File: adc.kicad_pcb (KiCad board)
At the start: 2 copper layers, 17 parts, among them U201 ADS8665IPWR

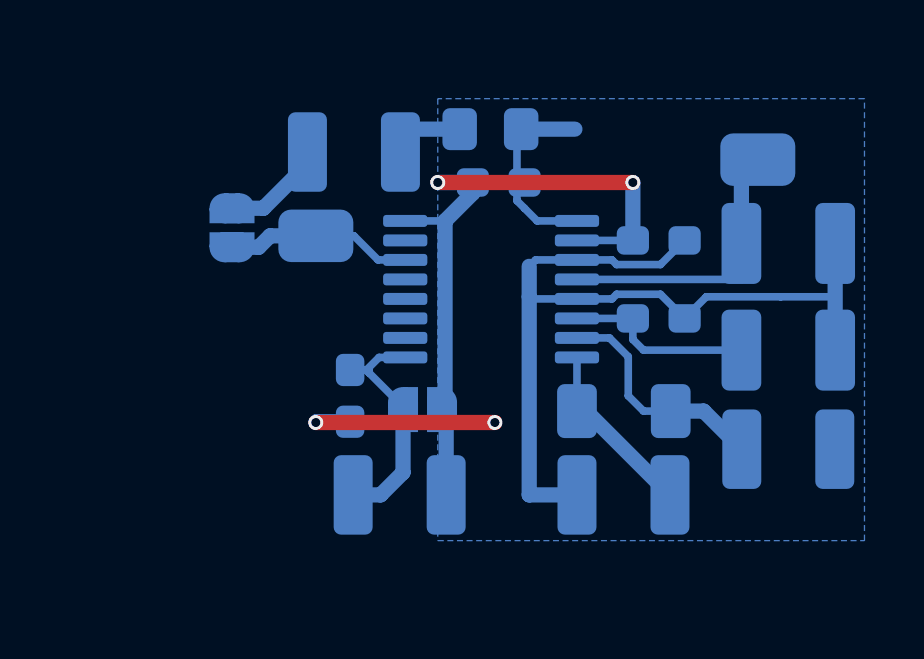
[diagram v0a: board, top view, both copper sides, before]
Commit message: add adc sub-layout
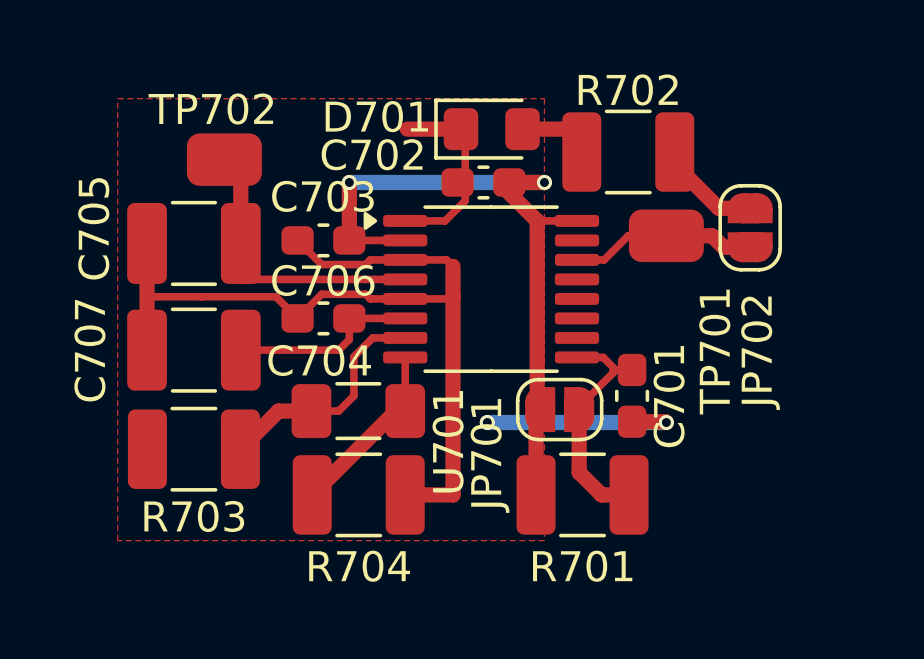
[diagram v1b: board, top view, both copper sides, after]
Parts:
- C701: renamed from C201; footprint pss:C_0603_1608Metric_Pad1.08x0.95mm_HandSolder -> meas:C_0603_1608Metric_Pad1.08x0.95mm_HandSolder; moved to F.Cu
- C702: renamed from C202; footprint pss:C_0603_1608Metric_Pad1.08x0.95mm_HandSolder -> meas:C_0603_1608Metric_Pad1.08x0.95mm_HandSolder; moved to F.Cu
- C703: renamed from C203; footprint pss:C_0603_1608Metric_Pad1.08x0.95mm_HandSolder -> meas:C_0603_1608Metric_Pad1.08x0.95mm_HandSolder; moved to F.Cu
- C704: renamed from C204; footprint pss:C_1206_3216Metric_Pad1.33x1.80mm_HandSolder -> meas:C_1206_3216Metric_Pad1.33x1.80mm_HandSolder; moved to F.Cu
- C705: renamed from C205; footprint pss:C_1210_3225Metric_Pad1.33x2.70mm_HandSolder -> meas:C_1210_3225Metric_Pad1.33x2.70mm_HandSolder; moved to F.Cu
- C706: renamed from C206; footprint pss:C_0603_1608Metric_Pad1.08x0.95mm_HandSolder -> meas:C_0603_1608Metric_Pad1.08x0.95mm_HandSolder; moved to F.Cu
- C707: renamed from C207; footprint pss:C_1210_3225Metric_Pad1.33x2.70mm_HandSolder -> meas:C_1210_3225Metric_Pad1.33x2.70mm_HandSolder; moved to F.Cu
- D701: renamed from D201; footprint pss:LED_0805_2012Metric_Pad1.15x1.40mm_HandSolder -> meas:LED_0805_2012Metric_Pad1.15x1.40mm_HandSolder; moved to F.Cu
- JP701: renamed from JP201; footprint pss:SolderJumper-2_P1.3mm_Open_RoundedPad1.0x1.5mm -> meas:SolderJumper-2_P1.3mm_Open_RoundedPad1.0x1.5mm; moved to F.Cu
- JP702: renamed from JP202; footprint pss:SolderJumper-2_P1.3mm_Bridged-Soldermask-Paste_RoundedPad1.0x1.5mm -> meas:SolderJumper-2_P1.3mm_Bridged-Soldermask-Paste_RoundedPad1.0x1.5mm; moved to F.Cu
- R701: renamed from R201; footprint pss:R_1210_3225Metric_Pad1.30x2.65mm_HandSolder -> meas:R_1210_3225Metric_Pad1.30x2.65mm_HandSolder; moved to F.Cu
- R702: renamed from R202; footprint pss:R_1210_3225Metric_Pad1.30x2.65mm_HandSolder -> meas:R_1210_3225Metric_Pad1.30x2.65mm_HandSolder; moved to F.Cu
- R703: renamed from R203; footprint pss:R_1210_3225Metric_Pad1.30x2.65mm_HandSolder -> meas:R_1210_3225Metric_Pad1.30x2.65mm_HandSolder; moved to F.Cu
- R704: renamed from R204; footprint pss:R_1210_3225Metric_Pad1.30x2.65mm_HandSolder -> meas:R_1210_3225Metric_Pad1.30x2.65mm_HandSolder; moved to F.Cu
- TP701: renamed from TP201; footprint pss:TP_0805_2012Metric -> meas:TP_0805_2012Metric; moved to F.Cu
- TP702: renamed from TP202; footprint pss:TP_0805_2012Metric -> meas:TP_0805_2012Metric; moved to F.Cu
- U701: renamed from U201; footprint pss:TSSOP-16_4.4x5mm_P0.65mm -> meas:TSSOP-16_4.4x5mm_P0.65mm; moved to F.Cu
- moved C705 19.8 mm to (65.3, 55.9), turned to 0 degrees
- moved C707 19.8 mm to (65.3, 59.4), turned to 0 degrees
- moved R703 19.8 mm to (65.3, 62.7), turned to 180 degrees
- moved TP702 17.8 mm to (66.3, 53.1), turned to 0 degrees
- moved JP702 17.3 mm to (83.8, 55.4)
- moved TP701 11.7 mm to (81.0, 55.6), turned to 0 degrees
- moved C703 11.2 mm to (69.6, 55.8), turned to 0 degrees
- moved C706 11.2 mm to (69.6, 58.4), turned to 0 degrees
- moved C701 9.40 mm to (79.9, 61.0)
- moved R702 9.14 mm to (79.8, 52.8), turned to 180 degrees
- moved C704 8.85 mm to (70.8, 61.5), turned to 180 degrees
- moved R704 8.83 mm to (70.8, 64.3), turned to 0 degrees
- moved R701 6.10 mm to (78.2, 64.3), turned to 0 degrees
- moved JP701 4.57 mm to (77.5, 61.4), turned to 0 degrees
- moved C702 0.51 mm to (74.9, 53.8), turned to 0 degrees
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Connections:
- net +5VA_adc renamed /+5VA_ADC
- net GND renamed /GND_ADC
- C701 pad 2: /~{RST} -> (no net)
- C704 pad 1: /AIN_GND -> (no net)
- C704 pad 2: /AIN_P_int -> (no net)
- C705 pad 2: /REFIO -> (no net)
- C706 pad 2: /REFCAP -> (no net)
- C707 pad 2: /REFCAP -> (no net)
- D701 pad 2: /GPO_LED -> (no net)
- JP701 pad 2: /~{RST} -> (no net)
- JP702 pad 1: /GPO_JMP -> (no net)
- JP702 pad 2: /GPO -> (no net)
- R701 pad 2: /~{RST} -> (no net)
- R702 pad 1: /GPO_JMP -> (no net)
- R702 pad 2: /GPO_LED -> (no net)
- R703 pad 1: /AIN_P_int -> (no net)
- R704 pad 1: /AIN_GND -> (no net)
- TP701 pad 1: /GPO -> (no net)
- TP702 pad 1: /REFIO -> (no net)
- U701 pad 14: /GPO -> (no net)
- U701 pad 4: /REFIO -> (no net)
- U701 pad 6: /REFCAP -> (no net)
- U701 pad 7: /AIN_P_int -> (no net)
- U701 pad 8: /AIN_GND -> (no net)
- U701 pad 9: /~{RST} -> (no net)
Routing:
- added copper zone on F.Cu, net /GND_ADC
- removed copper zone on B.Cu, net /GND_ADC
